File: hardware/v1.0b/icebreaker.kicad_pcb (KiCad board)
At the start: 4 copper layers, 73 x 37 mm, 128 parts, among them J1 Jumper, J10 Jumper, J11 Jumper, J12 Jumper, J13 Jumper, J14 Jumper, J15 Jumper, J16 Jumper, J17 Jumper, J18 Jumper, J19 Jumper, J2 Jumper, J20 Flash, J21 PMOD, J22 PMOD, J23 PMOD, J24 PMOD, J25 RGB Led, J26 5V AUX, J27 5V AUX, J28 CRESET, J3 Jumper, J4 Jumper, J5 Jumper, J6 Jumper, J7 Jumper, J8 Jumper, J9 Jumper, P1 pkl_USB_OTG, P2 UP, P3 UP, P4 UP, P5 UP, SW1 TACT, SW2 TACT, SW3 TACT, SW4 TACT, U1 93C46B-SOT-23-6, U2 3.3V, U3 1V2, U4 FT2232H, U5 W25Q, U6 ICE5LP4K-SG48, U7 12MHz

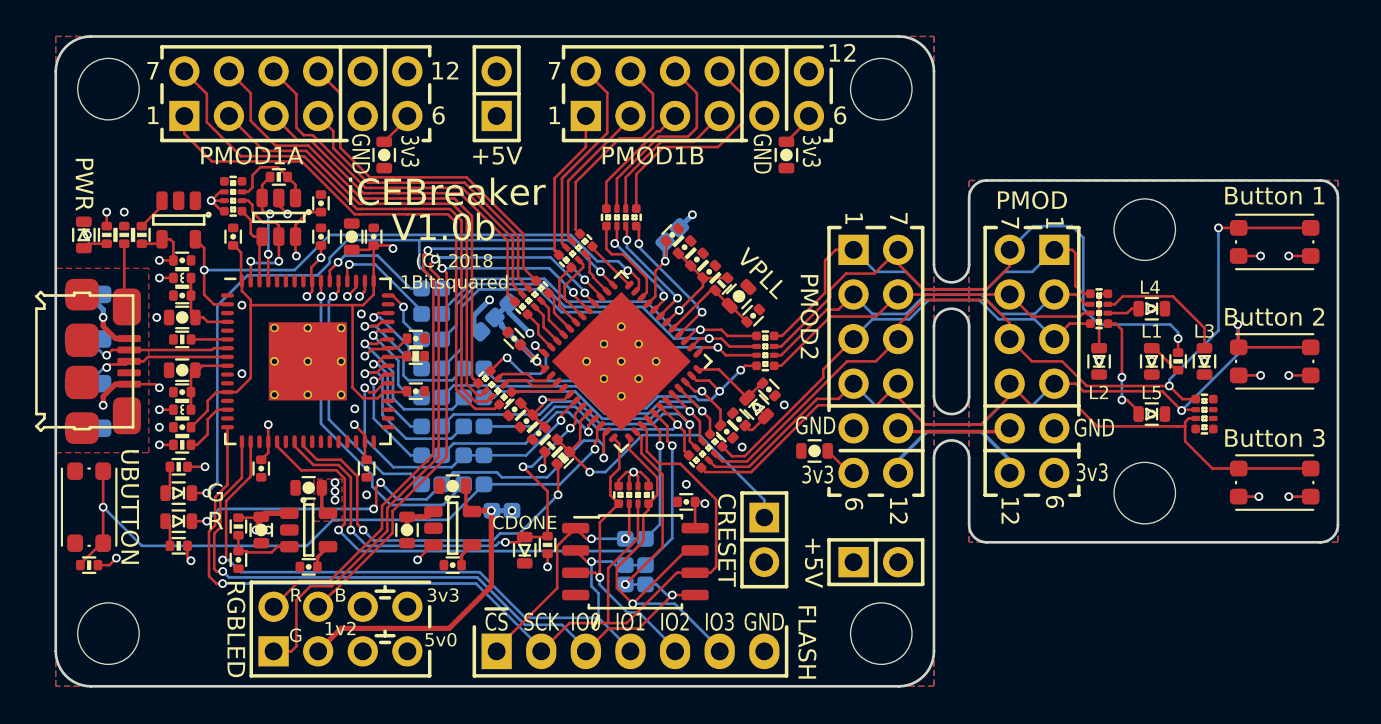
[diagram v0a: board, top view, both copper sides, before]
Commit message: Updated tact switch footprints to match the new parts. Closes #17
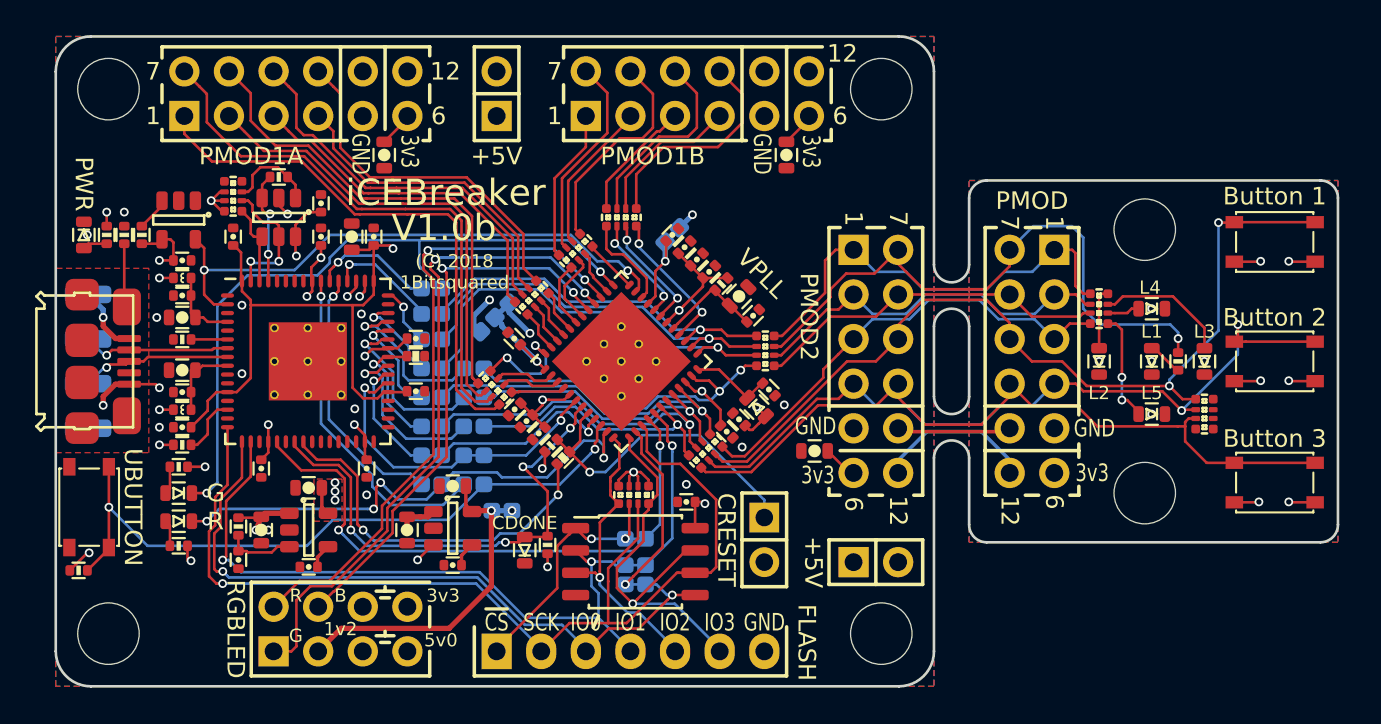
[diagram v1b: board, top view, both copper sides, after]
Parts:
- SW1, SW2, SW3, SW4: footprint pkl_buttons_switches:SW_SPST_KMR2 -> pkl_buttons_switches:SW_SPST_3x4x2.5
- moved R13 0.67 mm to (31.3, 59.4), turned to 180 degrees
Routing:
- net +3V3: track 66.6 -> 68.4 mm
- net /P2_9x: track 50.1 -> 50.7 mm
